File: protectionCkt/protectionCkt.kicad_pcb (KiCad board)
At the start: 2 copper layers, 50.9 x 33.2 mm, 13 parts, among them U1 282837-2, U2 282837-2, U3 SI1470DH-T1-E3, U4 LTC4361HTS8-2-TRMPBF, U5 282837-2

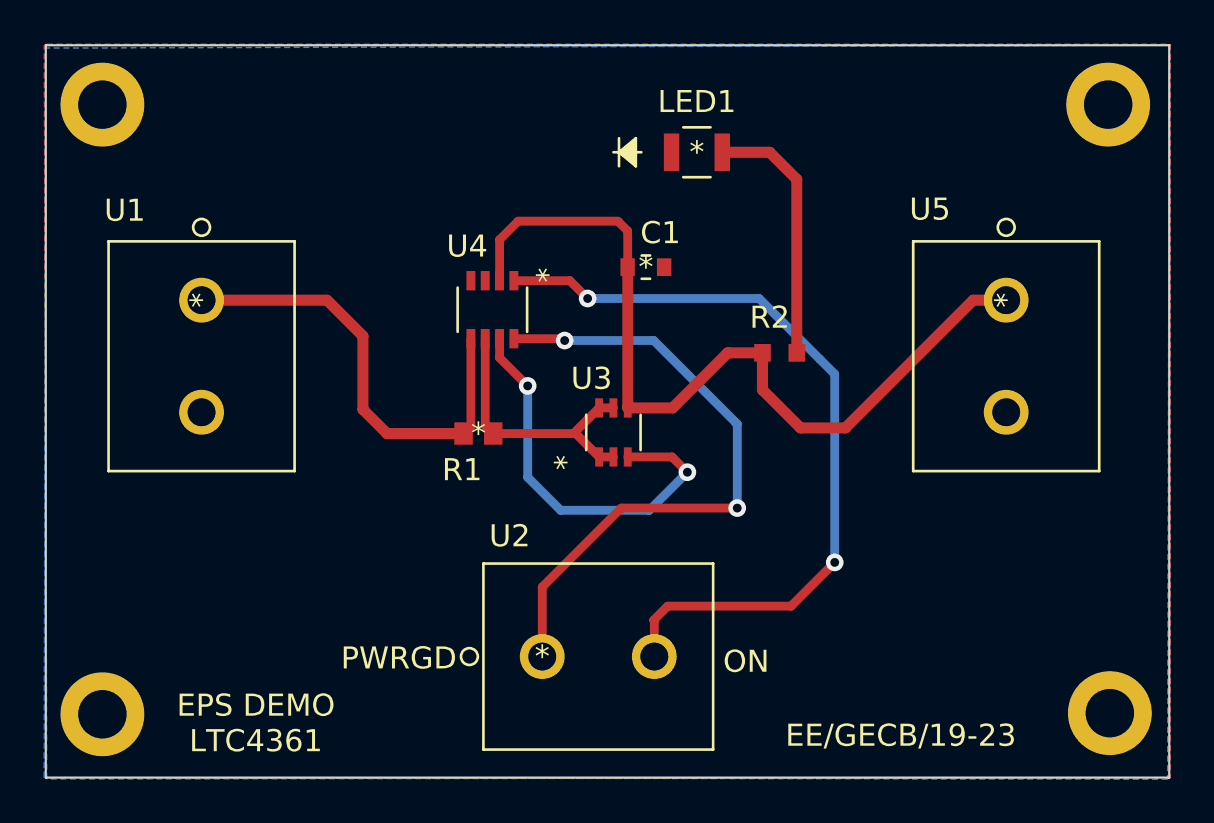
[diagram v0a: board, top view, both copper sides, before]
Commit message: updated pcb
reduced pcb size, added corner chamfer.
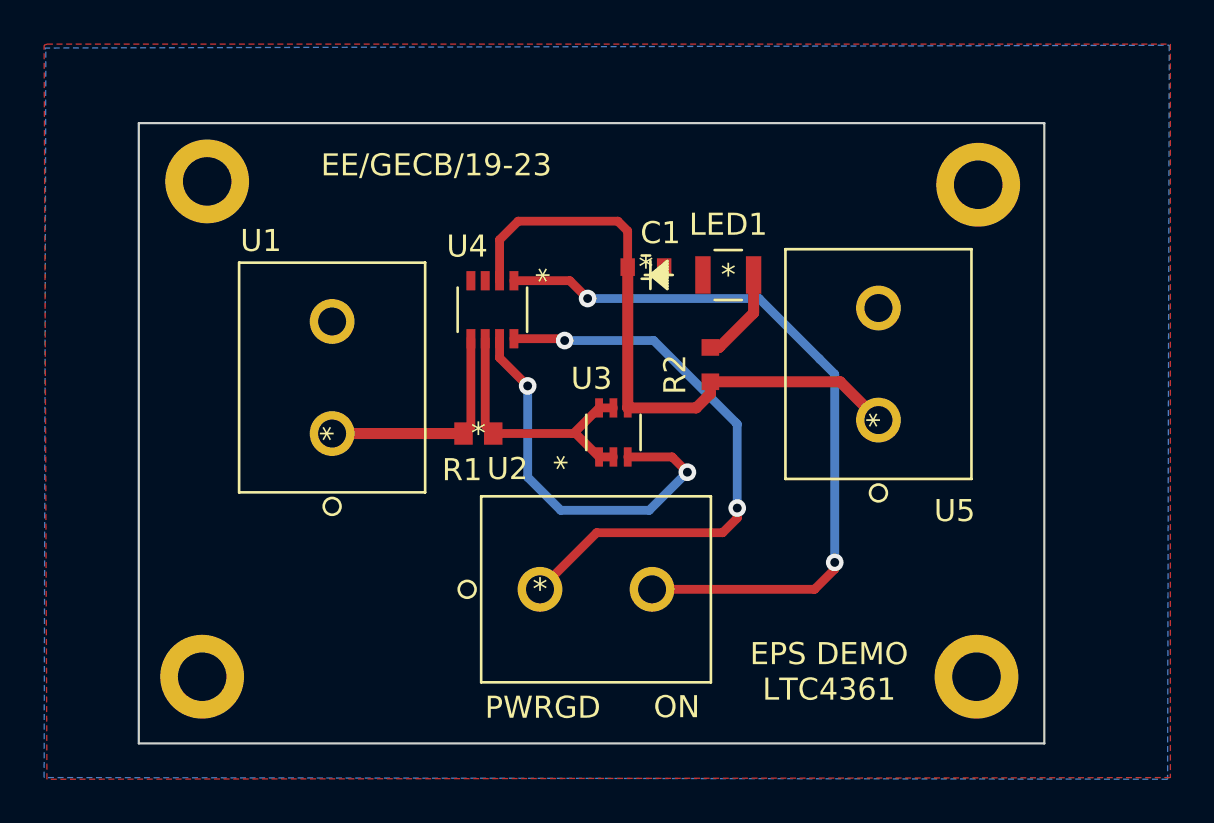
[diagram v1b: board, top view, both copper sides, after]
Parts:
- moved U1 8.46 mm to (124.7, 91.1), turned to 90 degrees
- moved U5 7.94 mm to (149.5, 90.5), turned to 90 degrees
- moved REF** 6.92 mm to (154.0, 79.8)
- moved REF** 6.27 mm to (153.9, 102.1)
- moved REF** 5.89 mm to (119.0, 79.7)
- moved LED1 5.74 mm to (142.7, 83.9)
- moved REF** 4.83 mm to (118.8, 102.1)
- moved R2 3.18 mm to (141.9, 88.0), turned to 90 degrees
- moved U2 3.05 mm to (134.1, 98.2)
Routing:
- net VCC: track 20.8 -> 10.4 mm
- net Net-(C1-Pad2): track 39.2 -> 29.1 mm
- net Net-(LED1-Pad2): track 11.8 -> 4.33 mm
- net Net-(U2-Pad1): track 29.0 -> 26.3 mm
- net Net-(U4-Pad1): track 35.8 -> 33.8 mm
- added copper zone on B.Cu, net GND
- removed copper zone on B.Cu, net (none)
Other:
- board size 50.9 x 33.2 mm -> 41 x 28.1 mm
